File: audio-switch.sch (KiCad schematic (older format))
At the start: 10 parts, among them U1 Pico

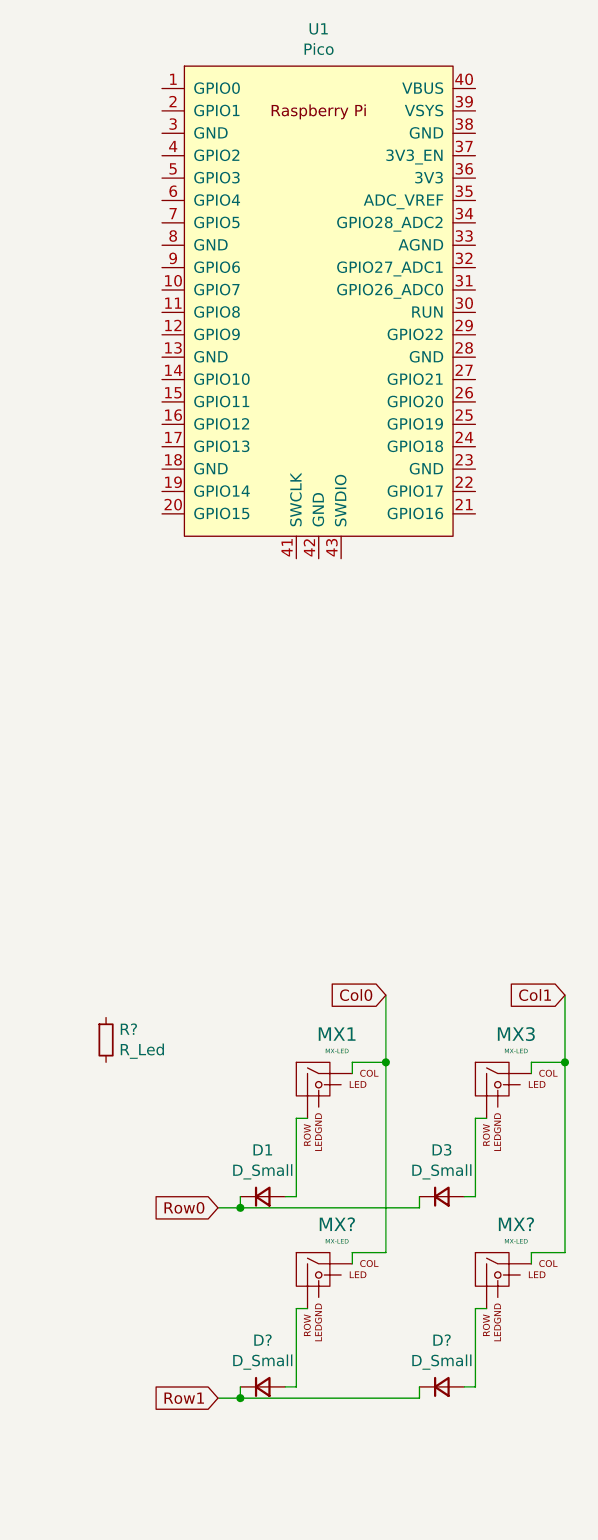
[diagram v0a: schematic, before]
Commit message: Wired switch and led matrix
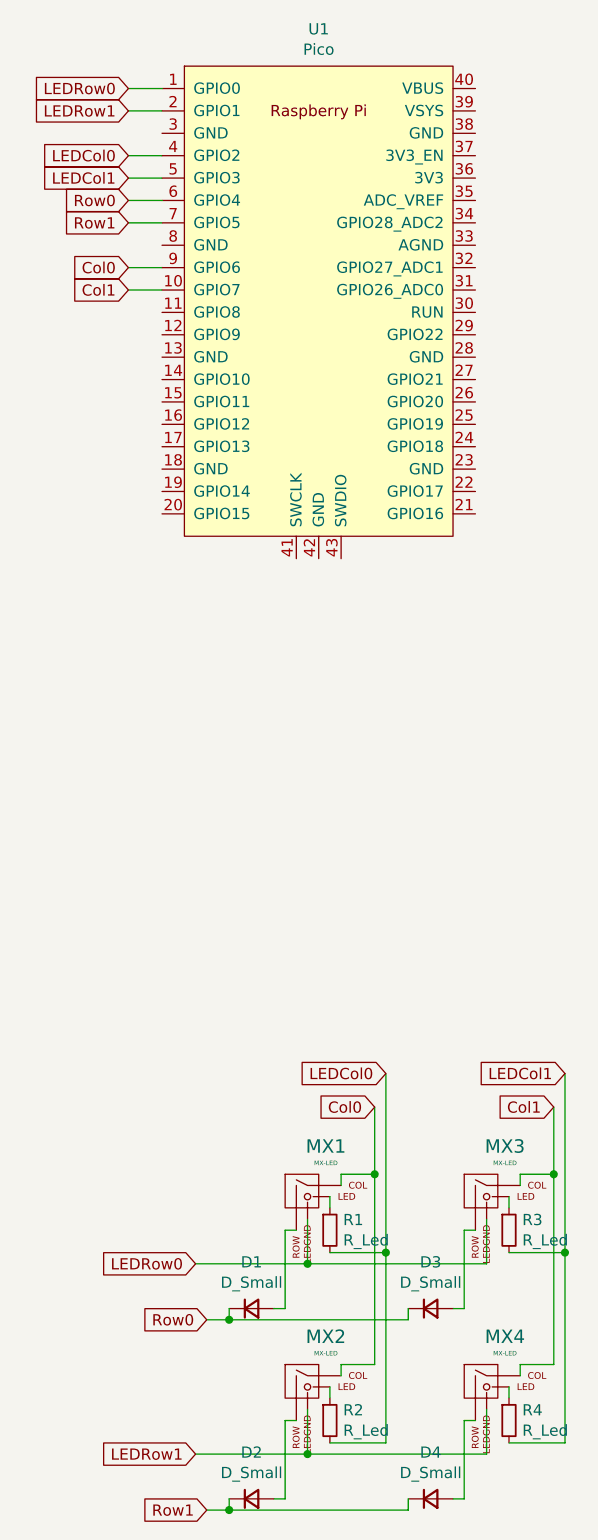
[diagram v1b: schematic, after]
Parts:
- added R1, R2, R3: R_Led, symbol Device:R_Small
- gave numbers to parts that had none: 5
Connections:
- net Col0: now also U1.9 (GPIO6)
- net Col1: now also U1.10 (GPIO7)
- net Row0: now also U1.6 (GPIO4)
- net Row1: now also U1.7 (GPIO5)
- net LEDRow0: now reaches U1.1 (GPIO0)
- net LEDRow0: now also MX1.4 (LEDGND), MX3.4 (LEDGND)
- net LEDRow1: now reaches U1.2 (GPIO1)
- net LEDRow1: now also MX2.4 (LEDGND), MX4.4 (LEDGND)
- net LEDCol0: now reaches U1.4 (GPIO2)
- net LEDCol0: now also R1.2, R2.2
- net LEDCol1: now reaches U1.5 (GPIO3)
- net LEDCol1: now also R4.2, R3.2
- net at MX1.3 (LED): now also R1.1
- net at MX3.3 (LED): now also R3.1
- net at MX2.3 (LED): now also R2.1
- net at MX4.3 (LED): now also R4.1
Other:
- moved on the sheet: D1, D2, D3, D4, MX1, MX2, MX3, MX4, R4

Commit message: Schematic maybe is done.
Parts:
- added J1, J2: AudioJack4_Out, Connector_Audio:Jack_3.5mm_PJ320E_Horizontal, symbol Connector:AudioJack4
- added J3, J4, J5, J6: AudioJack4_IN, Connector_Audio:Jack_3.5mm_PJ320E_Horizontal, symbol Connector:AudioJack4
- added U2, U3: CD4052B, Package_DIP:DIP-16_W7.62mm, symbol Analog_Switch:CD4052B
- D1, D2, D3, D4: footprint (none) -> Diode_SMD:D_0805_2012Metric_Pad1.15x1.40mm_HandSolder
- MX1, MX2, MX3, MX4: footprint (none) -> MX_Only:MXOnly-1U
- R1, R2, R3, R4: footprint (none) -> Resistor_SMD:R_0805_2012Metric_Pad1.20x1.40mm_HandSolder
- U1: footprint RPi_Pico:RPi_Pico_SMD_TH -> pi:RPi_Pico_SMD_TH
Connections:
- net GND: now reaches U1.13 (GND)
- net GND: now also U1.18 (GND), U1.23 (GND), U1.28 (GND), U1.3 (GND), U1.38 (GND), U1.8 (GND), U2.6 (INH), U2.8 (VSS), U3.6 (INH), U3.8 (VSS)
- net Select_A: now reaches U1.19 (GPIO14)
- net Select_A: now also U2.10 (A), U3.10 (A)
- net Select_B: now reaches U1.20 (GPIO15)
- net Select_B: now also U2.9 (B), U3.9 (B)
- net GNDA: now reaches U1.33 (AGND)
- net +3V3: now reaches U1.37 (3V3_EN)
- net +5V: now reaches U1.40 (VBUS)
- net +5V: now also U2.16 (VDD), U2.7 (VEE), U3.16 (VDD), U3.7 (VEE)
- new net: J3.R1, U2.12 (X0)
- new net: J3.R2, U3.1 (Y0)
- new net: J3.S, U3.12 (X0)
- new net: J3.T, U2.1 (Y0)
- new net: J4.R1, U2.14 (X1)
- new net: J4.R2, U3.5 (Y1)
- new net: J4.S, U3.14 (X1)
- new net: J4.T, U2.5 (Y1)
- new net: J5.R1, U2.15 (X2)
- new net: J5.R2, U3.2 (Y2)
- new net: J5.S, U3.15 (X2)
- new net: J5.T, U2.2 (Y2)
- new net: J6.R1, U2.11 (X3)
- new net: J6.R2, U3.4 (Y3)
- new net: J6.S, U3.11 (X3)
- new net: J6.T, U2.4 (Y3)
- new net Out_R1: J1.R1, J2.R1, U2.13 (X)
- new net Out_R2: J1.R2, J2.R2, U3.3 (Y)
- new net Out_S: J1.S, J2.S, U3.13 (X)
- new net Out_T: J1.T, J2.T, U2.3 (Y)

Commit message: Update
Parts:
- J1: value AudioJack4_Out -> OUT_1
- U2, U3: footprint Package_DIP:DIP-16_W7.62mm -> Package_DIP:DIP-16_W7.62mm_Socket
- renumbered J3 to IN_1, J4 to IN_2, J5 to IN_3, J6 to IN_4, J2 to OUT_2
